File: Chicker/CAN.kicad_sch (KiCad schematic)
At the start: 23 parts, among them J3 JST_BM04B-GHS-TBT, U6 SN65HVD233, U7 MCP2515-xST, Y2 ABM3-8.000MHZ-D2Y-T

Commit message: chicker v1.1 basic parts
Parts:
- D26: JLC C5331072 -> SOT-723; LCSC N/A -> C5331072
- L1: now not fitted; now left out of the parts list
- U6: LCSC C7376 -> C61643; now left out of the parts list
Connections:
- net CANH: now also U6.7 (CANH); no longer L1.1
- net CANL: now also U6.6 (CANL); no longer L1.3
- net CANH+: no longer names the net of L1.2
- net CANH+: no longer U6.7 (CANH)
- net CANL-: no longer names the net of L1.4
- net CANL-: no longer U6.6 (CANL)
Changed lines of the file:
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@@
 	(wire
 		(pts
-			(xy 63.5 96.52) (xy 72.39 96.52)
+			(xy 63.5 96.52) (xy 109.22 96.52)
 		)
 		(stroke
@@
 	(wire
 		(pts
-			(xy 68.58 91.44) (xy 72.39 91.44)
+			(xy 68.58 91.44) (xy 109.22 91.44)
 		)
 		(stroke
@@
 	(wire
 		(pts
-			(xy 82.55 91.44) (xy 109.22 91.44)
-		)
-		(stroke
-			(width 0)
-			(type default)
-		)
-	)
-	(wire
-		(pts
 			(xy 161.29 95.25) (xy 161.29 96.52)
 		)
@@
 		(pts
 			(xy 210.82 139.7) (xy 212.09 139.7)
-		)
-		(stroke
-			(width 0)
-			(type default)
-		)
-	)
-	(wire
-		(pts
-			(xy 82.55 96.52) (xy 109.22 96.52)
 		)
 		(stroke
@@
 		)
 	)
-	(label "CANH+"
-		(at 109.22 91.44 180)
-		(effects
-			(font
-				(size 1.27 1.27)
-			)
-			(justify right bottom)
-		)
-	)
 	(label "RXCAN"
 		(at 135.89 91.44 0)
@@
 		)
 	)
+	(label "CAN+"
+		(at 106.68 91.44 180)
+		(effects
+			(font
+				(size 1.27 1.27)
+			)
+			(justify right bottom)
+		)
+	)
 	(label "Rs"
 		(at 137.16 99.06 0)
@@
 		)
 	)
-	(label "CAN+"
-		(at 36.83 91.44 180)
-		(effects
-			(font
-				(size 1.27 1.27)
-			)
-			(justify right bottom)
-		)
-	)
 	(label "SPI0_RX"
 		(at 208.28 77.47 180)
@@
 		)
 	)
-	(label "CANL-"
-		(at 109.22 96.52 180)
-		(effects
-			(font
-				(size 1.27 1.27)
-			)
-			(justify right bottom)
-		)
-	)
 	(label "OSC2"
 		(at 204.47 95.25 180)
@@
 	)
 	(label "CAN-"
-		(at 36.83 96.52 180)
+		(at 106.68 96.52 180)
 		(effects
 			(font
@@
 		(unit 1)
 		(exclude_from_sim no)
-		(in_bom yes)
+		(in_bom no)
 		(on_board yes)
 		(dnp no)
@@
 			)
 		)
-		(property "LCSC" "C7376"
+		(property "LCSC" "C61643"
 			(at 121.92 93.98 0)
 			(effects
@@
 			)
 		)
-		(property "Description" "Zener diode"
+		(property "Description" "Zener diode ESD"
 			(at 66.04 101.6 0)
 			(effects
@@
 			)
 		)
-		(property "JLC" "C5331072"
+		(property "JLC" "SOT-723"
 			(at 63.5 101.6 0)
 			(effects
@@
 			)
 		)
-		(property "LCSC" "N/A"
+		(property "LCSC" "C5331072"
 			(at 60.96 104.14 0)
 			(effects
@@
 	(symbol
 		(lib_id "bots:L_Coupled")
-		(at 77.47 93.98 0)
+		(at 74.93 77.47 0)
 		(unit 1)
-		(exclude_from_sim no)
-		(in_bom yes)
-		(on_board yes)
-		(dnp no)
+		(exclude_from_sim yes)
+		(in_bom no)
+		(on_board no)
+		(dnp yes)
 		(fields_autoplaced yes)
 		(property "Reference" "L1"
-			(at 77.089 86.36 0)
+			(at 74.549 69.85 0)
 			(effects
 				(font
@@
 		)
 		(property "Value" "L_Coupled"
-			(at 77.089 88.9 0)
+			(at 74.549 72.39 0)
 			(effects
 				(font
@@
 		)
 		(property "Footprint" ""
-			(at 77.47 93.98 0)
+			(at 74.93 77.47 0)
 			(effects
 				(font
@@
 		)
 		(property "Datasheet" "~"
-			(at 77.47 93.98 0)
+			(at 74.93 77.47 0)
 			(effects
 				(font
@@
 		)
 		(property "Description" "Coupled inductor"
-			(at 77.47 93.98 0)
+			(at 74.93 77.47 0)
 			(effects
 				(font
@@
 		)
 		(instances
-			(project ""
+			(project "chicker"
 				(path "/1a9ce3e8-a091-496c-9c5f-e7b2eb60e275/1021984a-8e05-406d-9dd0-ca39eed7d7ab"
 					(reference "L1")

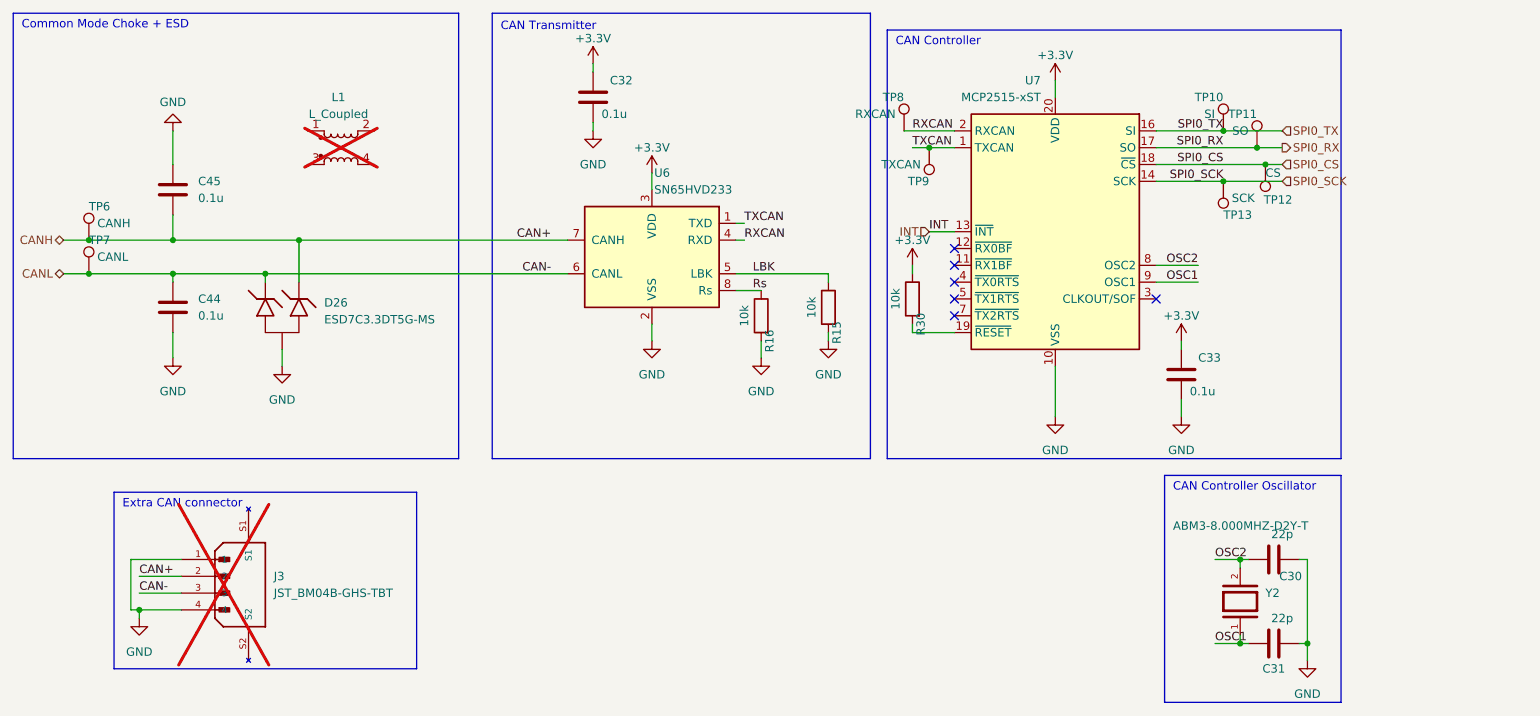
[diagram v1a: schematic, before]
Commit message: changed more to basic
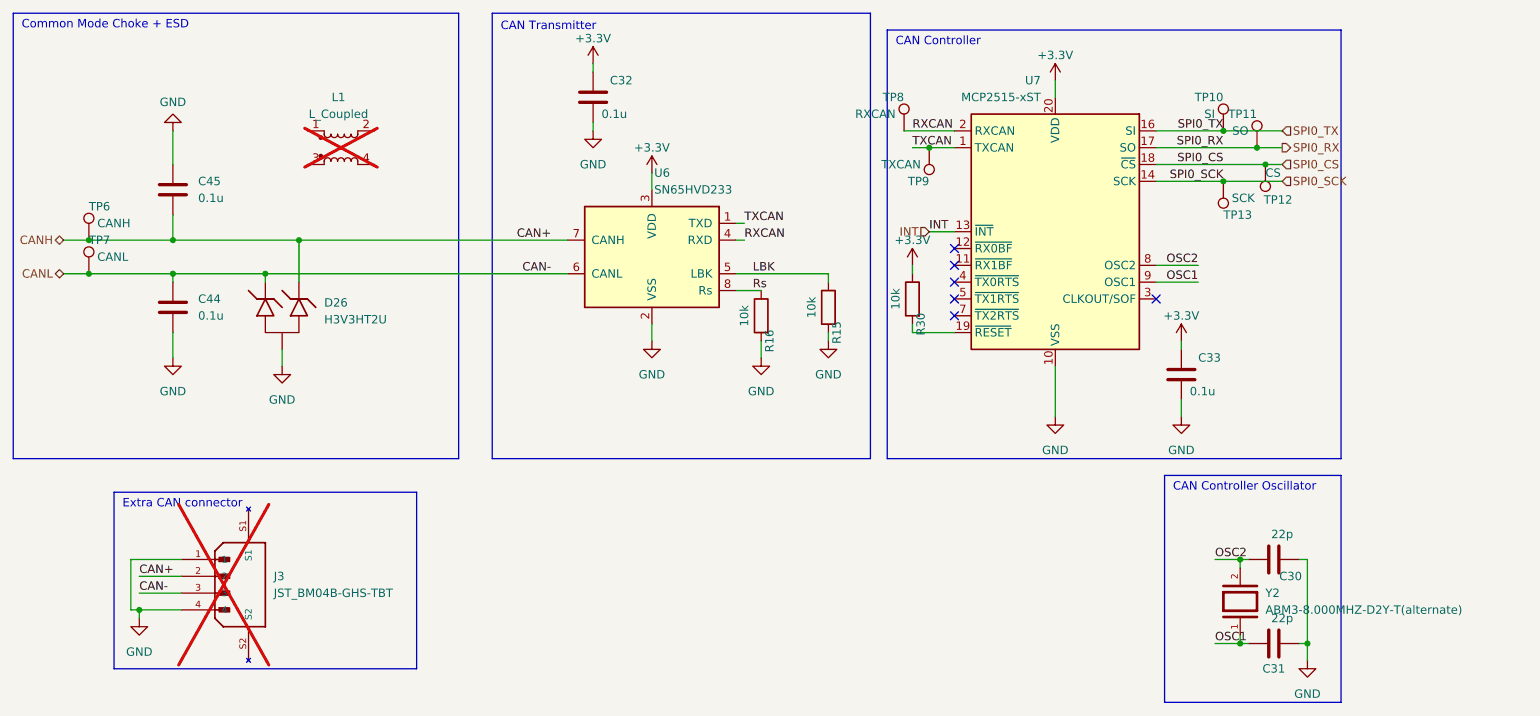
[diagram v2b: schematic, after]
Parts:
- removed Y2: ABM3-8.000MHZ-D2Y-T, bots:ABM3, symbol bots:ABM3-8.000MHZ-D2Y-T
- added Y2: ABM3-8.000MHZ-D2Y-T(alternate), bots:ABM3, symbol bots:XTAL-8MHZ-YXC
- D26: value ESD7C3.3DT5G-MS -> H3V3HT2U; JLC SOT-723 -> SOT-23; LCSC C5331072 -> C20617924; MPN ESD7C3.3DT5G-MS -> H3V3HT2U; Manufacturer Micro Commercial Co -> hongjiacheng; Price 0.63 -> 0.0379
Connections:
- net OSC1: now also Y2.1
- net OSC2: now also Y2.2
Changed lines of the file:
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@@
 			)
 		)
-		(property "Value" "ESD7C3.3DT5G-MS"
+		(property "Value" "H3V3HT2U"
 			(at 72.39 103.4414 90)
 			(effects
@@
 			)
 		)
-		(property "MPN" "ESD7C3.3DT5G-MS "
+		(property "MPN" "H3V3HT2U"
 			(at 59.69 105.41 0)
 			(effects
@@
 			)
 		)
-		(property "Manufacturer" "Micro Commercial Co"
+		(property "Manufacturer" "hongjiacheng"
 			(at 60.96 104.14 0)
 			(effects
@@
 			)
 		)
-		(property "Price" "0.63"
+		(property "Price" "0.0379"
 			(at 60.96 104.14 0)
 			(effects
@@
 			)
 		)
-		(property "JLC" "SOT-723"
+		(property "JLC" "SOT-23"
 			(at 63.5 101.6 0)
 			(effects
@@
 			)
 		)
-		(property "LCSC" "C5331072"
+		(property "LCSC" "C20617924 "
 			(at 60.96 104.14 0)
 			(effects
@@
 	)
 	(symbol
+		(lib_id "bots:XTAL-8MHZ-YXC")
+		(at 210.82 146.05 90)
+		(unit 1)
+		(exclude_from_sim no)
+		(in_bom yes)
+		(on_board yes)
+		(dnp no)
+		(fields_autoplaced yes)
+		(property "Reference" "Y2"
+			(at 214.63 144.7799 90)
+			(effects
+				(font
+					(size 1.27 1.27)
+				)
+				(justify right)
+			)
+		)
+		(property "Value" "ABM3-8.000MHZ-D2Y-T(alternate)"
+			(at 214.63 147.3199 90)
+			(effects
+				(font
+					(size 1.27 1.27)
+				)
+				(justify right)
+			)
+		)
+		(property "Footprint" "bots:ABM3"
+			(at 210.82 146.05 0)
+			(effects
+				(font
+					(size 1.27 1.27)
+				)
+				(justify bottom)
+				(hide yes)
+			)
+		)
+		(property "Datasheet" ""
+			(at 210.82 146.05 0)
+			(effects
+				(font
+					(size 1.27 1.27)
+				)
+				(hide yes)
+			)
+		)
+		(property "Description" ""
+			(at 210.82 146.05 0)
+			(effects
+				(font
+					(size 1.27 1.27)
+				)
+				(hide yes)
+			)
+		)
+		(property "MPN" " X50328MSB2GI"
+			(at 210.82 146.05 0)
+			(effects
+				(font
+					(size 1.27 1.27)
+				)
+				(justify bottom)
+				(hide yes)
+			)
+		)
+		(property "Manufacturer" "YXC Crystal Oscillators"
+			(at 210.82 146.05 0)
+			(effects
+				(font
+					(size 1.27 1.27)
+				)
+				(justify bottom)
+				(hide yes)
+			)
+		)
+		(property "Price" "0.20"
+			(at 210.82 146.05 0)
+			(effects
+				(font
+					(size 1.27 1.27)
+				)
+				(hide yes)
+			)
+		)
+		(property "JLC" "SMD5032"
+			(at 210.82 146.05 0)
+			(effects
+				(font
+					(size 1.27 1.27)
+				)
+				(hide yes)
+			)
+		)
+		(property "LCSC" "C115962"
+			(at 210.82 146.05 0)
+			(effects
+				(font
+					(size 1.27 1.27)
+				)
+				(hide yes)
+			)
+		)
+		(property "JLC Extended" "no"
+			(at 210.82 146.05 0)
+			(effects
+				(font
+					(size 1.27 1.27)
+				)
+				(hide yes)
+			)
+		)
+		(pin "1"
+		)
+		(pin "2"
+		)
+		(instances
+			(project ""
+				(path "/1a9ce3e8-a091-496c-9c5f-e7b2eb60e275/1021984a-8e05-406d-9dd0-ca39eed7d7ab"
+					(reference "Y2")
+					(unit 1)
+				)
+			)
+		)
+	)
+	(symbol
 		(lib_id "bots:C_0.1u")
 		(at 201.93 111.76 0)
@@
 					(unit 1)
 				)
-			)
-		)
-	)
-	(symbol
-		(lib_id "bots:ABM3-8.000MHZ-D2Y-T")
-		(at 210.82 146.05 90)
-		(unit 1)
-		(exclude_from_sim no)
-		(in_bom yes)
-		(on_board yes)
-		(dnp no)
-		(property "Reference" "Y2"
-			(at 214.63 144.78 90)
-			(effects
-				(font
-					(size 1.27 1.27)
-				)
-				(justify right)
-			)
-		)
-		(property "Value" "ABM3-8.000MHZ-D2Y-T"
-			(at 200.66 134.62 90)
-			(effects
-				(font
-					(size 1.27 1.27)
-				)
-				(justify right)
-			)
-		)
-		(property "Footprint" "bots:ABM3"
-			(at 210.82 146.05 0)
-			(effects
-				(font
-					(size 1.27 1.27)
-				)
-				(justify bottom)
-				(hide yes)
-			)
-		)
-		(property "Datasheet" ""
-			(at 210.82 146.05 0)
-			(effects
-				(font
-					(size 1.27 1.27)
-				)
-				(hide yes)
-			)
-		)
-		(property "Description" ""
-			(at 210.82 146.05 0)
-			(effects
-				(font
-					(size 1.27 1.27)
-				)
-				(hide yes)
-			)
-		)
-		(property "MPN" "ABM3-8.000MHZ-D2Y-T"
-			(at 210.82 146.05 0)
-			(effects
-				(font
-					(size 1.27 1.27)
-				)
-				(justify bottom)
-				(hide yes)
-			)
-		)
-		(property "Price" "0.2279"
-			(at 210.82 146.05 0)
-			(effects
-				(font
-					(size 1.27 1.27)
-				)
-				(hide yes)
-			)
-		)
-		(property "JLC" "SMD5032-2P"
-			(at 210.82 146.05 0)
-			(effects
-				(font
-					(size 1.27 1.27)
-				)
-				(hide yes)
-			)
-		)
-		(property "LCSC" "C144380"
-			(at 210.82 146.05 0)
-			(effects
-				(font
-					(size 1.27 1.27)
-				)
-				(hide yes)
-			)
-		)
-		(property "MANUFACTURER" "Cardinal Components"
-			(at 210.82 146.05 0)
-			(effects
-				(font
-					(size 1.27 1.27)
-				)
-				(justify bottom)
-				(hide yes)
-			)
-		)
-		(property "Manufacturer" "Cardinal Components"
-			(at 210.82 146.05 0)
-			(effects
-				(font
-					(size 1.27 1.27)
-				)
-				(justify bottom)
-				(hide yes)
-			)
-		)
-		(property "JLC Extended" "yes"
-			(at 210.82 146.05 0)
-			(effects
-				(font
-					(size 1.27 1.27)
-				)
-				(hide yes)
-			)
-		)
-		(pin "1"
-		)
-		(pin "2"
-		)
-		(instances
-			(project "chicker"
-				(path "/1a9ce3e8-a091-496c-9c5f-e7b2eb60e275/1021984a-8e05-406d-9dd0-ca39eed7d7ab"
-					(reference "Y2")
-					(unit 1)
-				)

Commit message: chicker v1.1 ordered!
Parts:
- D26: footprint bots:SOT-723 -> bots:SOT-23
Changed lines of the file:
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@@
 			)
 		)
-		(property "Footprint" "bots:SOT-723"
+		(property "Footprint" "bots:SOT-23"
 			(at 59.69 105.41 0)
 			(effects

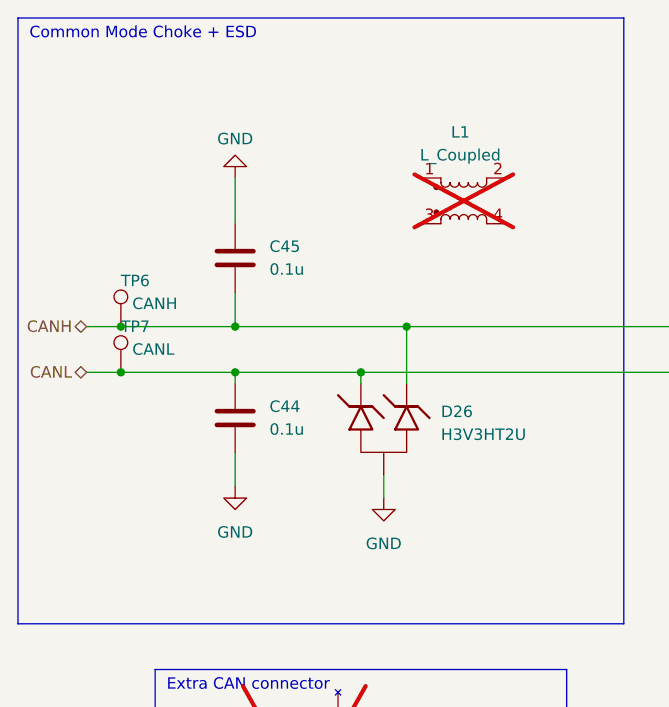
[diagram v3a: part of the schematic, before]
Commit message: damping can bus code
+ changing charging to every 5s
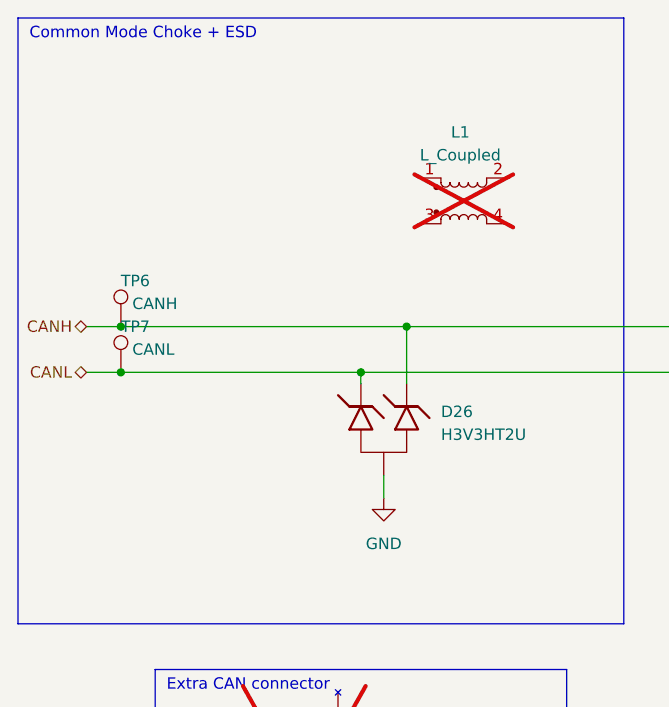
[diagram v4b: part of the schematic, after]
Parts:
- removed C44, C45: 0.1u, bots:C_0603_1608Metric, symbol bots:C_0.1u
